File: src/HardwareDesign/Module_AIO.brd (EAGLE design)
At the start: 55 x 110 mm, 343 parts, among them IC1 MIC5504-3.3YM5-TR, IC10 ADS9234RIRHBR, IC11 AD8605, IC12 MCP1525T-I/TT, IC13 AD8605, IC14 TPS65131, IC15 TPS7A39, IC16 SN74LVC2G66, IC17 74LVC1G04, IC2 RP2040, IC22 DAC8568, IC23 AD8605, IC24 OPA192, IC25 OPA192, IC26 OPA192, IC27 OPA192, IC28 OPA197, IC29 OPA197, IC3 MCP6001AIDBVRG, IC30 OPA197, IC31 OPA197, IC4 W25Q128JVPIQ, IC6 DG409, IC7 ADA4254ACPZ, IC8 DG409, IC9 ADA4254ACPZ, T2 IRLML5203, X1 CON-VG_MAB64, X2 K5A1200015304P

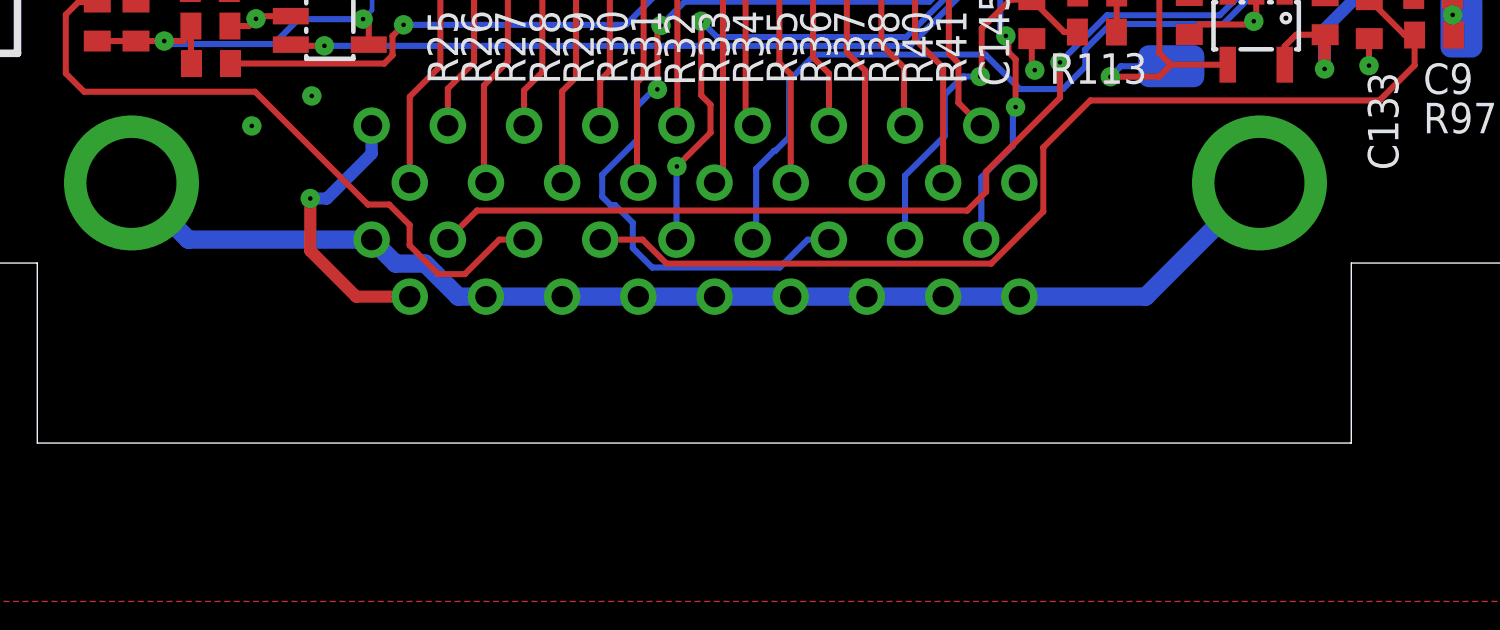
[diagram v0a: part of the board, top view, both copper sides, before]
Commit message: finish DIO card desing
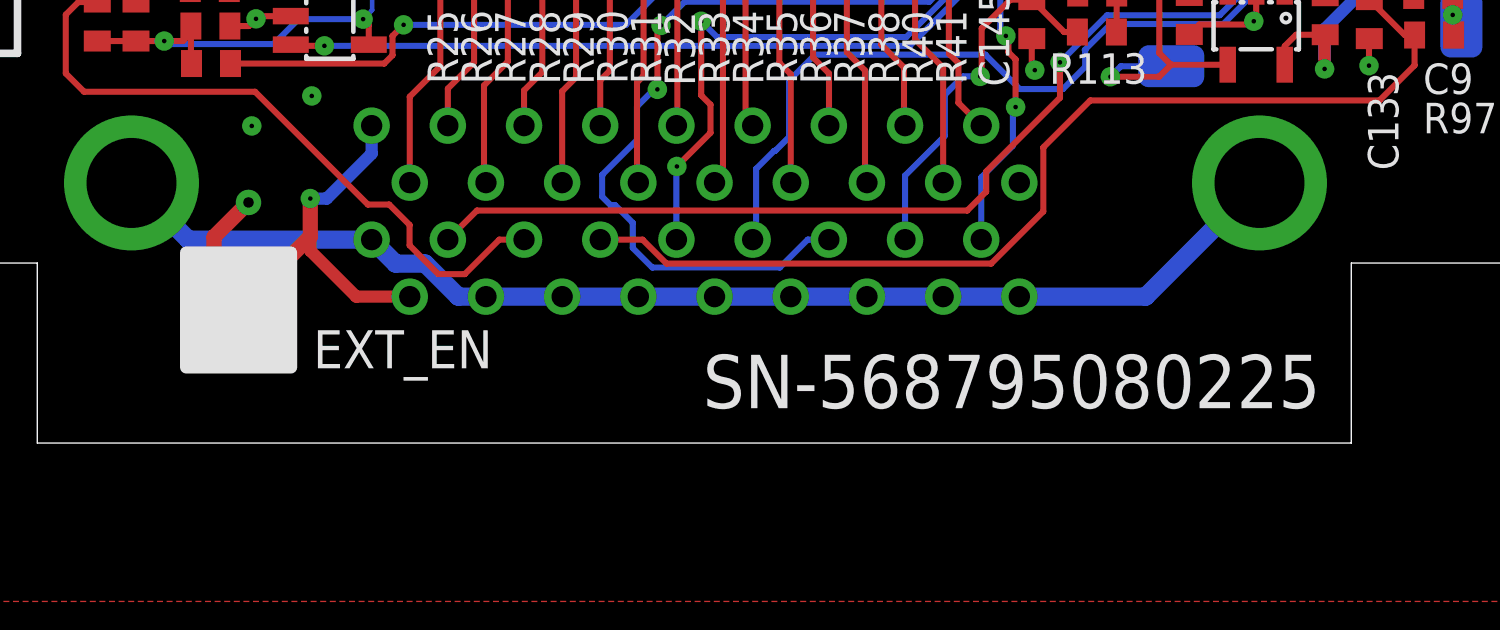
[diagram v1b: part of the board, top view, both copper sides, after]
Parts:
- added JP-EXT-1, JP-EXT-2: 0R, ds_passive:0603
- R72, R77: value 4.7K -> 10K
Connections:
- net +5V: now also JP-EXT-1.1, JP-EXT-2.1
- net EXT: now also JP-EXT-1.2, JP-EXT-2.2
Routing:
- net +5V: track 243.6 -> 259.3 mm, vias 11 -> 12
- net EXT: track 9.29 -> 14.5 mm
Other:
- board text added: "EXT_EN"
- board text added: "SN-568795080225"
- board text removed: "SN-070225-0539"
